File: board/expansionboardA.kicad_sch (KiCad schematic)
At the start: 58 parts, among them IC1 IS61WV25616EDBLL-10TLI, J1 USB_C_Receptacle, J2 USB_A_Stacked, J3 HDMI_A, J4 FAN, J5 DEBUG, U1 MAX3420EECJ, U2 GPIO_U2, U4 GPIO_U4, U6 CS4344-CZZR, U7 MAX3421EEHJ+T, Y1 Crystal, Y2 Crystal

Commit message: Updated board files
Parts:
- removed IC1: IS61WV25616EDBLL-10TLI, SOP80P1176X120-44N, symbol IS61WV25616EDBLL-10TLI:IS61WV25616EDBLL-10TLI
- added JP1: Jumper_2_Open, Jumper:SolderJumper-2_P1.3mm_Open_RoundedPad1.0x1.5mm, symbol Jumper:Jumper_2_Open
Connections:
- net 5V: now also JP1.2 (B)
- net GND: now also J3.11 (CKS), J3.2 (D2S), J3.5 (D1S), J3.8 (D0S), J3.SH
- net RIGHTOUT: no longer LSRIGHT1.P
- net speakerout: now reaches AU1.2, C9.1, R8.2
- net speakerout: now also LSRIGHT1.P
- net SRA0: no longer names the net of U2.34 (Pin_34)
- net SRA1: no longer names the net of U2.33 (Pin_33)
- net SRA10: no longer names the net of U4.10 (Pin_10)
- net SRA11: no longer names the net of U4.9 (Pin_9)
- net SRA12: no longer names the net of U4.12 (Pin_12)
- net SRA13: no longer names the net of U4.11 (Pin_11)
- net SRA14: no longer names the net of U4.14 (Pin_14)
- net SRA15: no longer names the net of U4.26 (Pin_26)
- net SRA16: no longer names the net of U4.25 (Pin_25)
- net SRA17: no longer names the net of U4.28 (Pin_28)
- net SRA2: no longer names the net of U2.32 (Pin_32)
- net SRA3: no longer names the net of U2.31 (Pin_31)
- net SRA4: no longer names the net of U2.30 (Pin_30)
- net SRA5: no longer names the net of U2.19 (Pin_19)
- net SRA6: no longer names the net of U2.18 (Pin_18)
- net SRA7: no longer names the net of U2.17 (Pin_17)
- net SRA8: no longer names the net of U2.16 (Pin_16)
- net SRA9: no longer names the net of U2.15 (Pin_15)
- net SRCEn: no longer names the net of U2.29 (Pin_29)
- net SRD0: no longer names the net of U2.28 (Pin_28)
- net SRD1: no longer names the net of U2.27 (Pin_27)
- net SRD10: no longer names the net of U4.15 (Pin_15)
- net SRD11: no longer names the net of U4.18 (Pin_18)
- net SRD12: no longer names the net of U4.17 (Pin_17)
- net SRD13: no longer names the net of U4.20 (Pin_20)
- net SRD14: no longer names the net of U4.19 (Pin_19)
- net SRD15: no longer names the net of U4.22 (Pin_22)
- net SRD2: no longer names the net of U2.26 (Pin_26)
- net SRD3: no longer names the net of U2.25 (Pin_25)
- net SRD4: no longer names the net of U2.24 (Pin_24)
- net SRD5: no longer names the net of U2.23 (Pin_23)
- net SRD6: no longer names the net of U2.22 (Pin_22)
- net SRD7: no longer names the net of U2.21 (Pin_21)
- net SRD8: no longer names the net of U4.13 (Pin_13)
- net SRD9: no longer names the net of U4.16 (Pin_16)
- net SRLB: no longer names the net of U4.21 (Pin_21)
- net SROE: no longer names the net of U4.23 (Pin_23)
- net SRUB: no longer names the net of U4.24 (Pin_24)
- net SRWE: no longer names the net of U2.20 (Pin_20)
- net n/c: no longer names the net of J3.18 (+5V)
- net n/c: now also JP1.1 (A)
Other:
- note removed: "SRAM"

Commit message: Board issue 2A with HDMI chip
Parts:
- removed JP1: Jumper_2_Open, Jumper:SolderJumper-2_P1.3mm_Open_RoundedPad1.0x1.5mm, symbol Jumper:Jumper_2_Open
- added JP1, JP2, JP3, JP4, JP5: Jumper_3_Open, Jumper:SolderJumper-3_P1.3mm_Open_RoundedPad1.0x1.5mm, symbol Jumper:Jumper_3_Open
- added R15, R18, R19, R20, R21, R22: 10KOhm, Resistor_SMD:R_0603_1608Metric_Pad0.98x0.95mm_HandSolder, symbol Device:R
- added R23: 33KOhm, Resistor_SMD:R_0603_1608Metric_Pad0.98x0.95mm_HandSolder, symbol Device:R
- added R24: 510Ohm, Resistor_SMD:R_0603_1608Metric_Pad0.98x0.95mm_HandSolder, symbol Device:R
- added U3: SII164CTG64, SI164CTG64:QFP50P1200X1200X120-64N, symbol SII164CTG64:SII164CTG64
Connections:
- net 5V: now also JP1.3 (B)
- net CK_N: now also U3.21 (TXC-); no longer U4.50 (Pin_50)
- net CK_P: now also U3.22 (TXC+); no longer U4.49 (Pin_49)
- net D0_N: now also U3.24 (TX0-); no longer U4.52 (Pin_52)
- net D0_P: now also U3.25 (TX0+); no longer U4.51 (Pin_51)
- net D1_N: now also U3.27 (TX1-); no longer U4.48 (Pin_48)
- net D1_P: now also U3.28 (TX1+); no longer U4.47 (Pin_47)
- net D2_N: now also U3.30 (TX2-); no longer U4.46 (Pin_46)
- net D2_P: now also U3.31 (TX2+); no longer U4.45 (Pin_45)
- net GND: now also JP2.1 (A), JP3.1 (A), JP4.1 (A), JP5.3 (B), R15.2, R19.2, U3.16 (GND), U3.17 (PGND), U3.20 (AGND), U3.26 (AGND__1), U3.32 (AGND__2), U3.48 (GND__1), U3.56 (IDCK-), U3.64 (GND__2)
- net REG3V3: now also JP1.1 (A), JP2.3 (B), JP3.3 (B), JP4.3 (B), R18.1, R20.2, R21.2, R22.2, R23.2, R24.2, U3.1 (VCC), U3.12 (VCC__1), U3.18 (PVCC1), U3.23 (AVCC), U3.29 (AVCC__1), U3.33 (VCC__2), U3.49 (PVCC2)
- net VRSTN: now reaches U4.12 (Pin_12)
- net VSCL: now reaches U4.14 (Pin_14)
- net VSDA: now reaches U4.16 (Pin_16)
- net VHOTPLUG: now reaches U4.18 (Pin_18)
- net VDKEN: now reaches U4.20 (Pin_20)
- net VDAT23: now reaches U4.25 (Pin_25)
- net VDAT23: now also U3.36 (D23)
- net VDAT22: now reaches U4.26 (Pin_26)
- net VDAT22: now also U3.37 (D22)
- net VDAT21: now reaches U4.27 (Pin_27)
- net VDAT21: now also U3.38 (D21)
- net VDAT20: now reaches U4.28 (Pin_28)
- net VDAT20: now also U3.39 (D20)
- net VDAT19: now reaches U4.29 (Pin_29)
- net VDAT19: now also U3.40 (D19)
- net VDAT18: now reaches U4.30 (Pin_30)
- net VDAT18: now also U3.41 (D18)
- net VDAT17: now reaches U4.31 (Pin_31)
- net VDAT17: now also U3.42 (D17)
- net VDAT16: now reaches U4.32 (Pin_32)
- net VDAT16: now also U3.43 (D16)
- net VDAT15: now reaches U4.33 (Pin_33)
- net VDAT15: now also U3.44 (D15)
- net VDAT14: now reaches U4.34 (Pin_34)
- net VDAT14: now also U3.45 (D14)
- net VDAT13: now reaches U4.35 (Pin_35)
- net VDAT13: now also U3.46 (D13)
- net VDAT12: now reaches U4.36 (Pin_36)
- net VDAT12: now also U3.47 (D12)
- net VDAT11: now reaches U4.37 (Pin_37)
- net VDAT11: now also U3.50 (D11)
- net VDAT10: now reaches U4.38 (Pin_38)
- net VDAT10: now also U3.51 (D10)
- net VDAT9: now reaches U4.39 (Pin_39)
- net VDAT9: now also U3.52 (D9)
- net VDAT8: now reaches U4.40 (Pin_40)
- net VDAT8: now also U3.53 (D8)
- net VDAT7: now reaches U4.41 (Pin_41)
- net VDAT7: now also U3.54 (D7)
- net VDAT6: now reaches U4.42 (Pin_42)
- net VDAT6: now also U3.55 (D6)
- net VDAT5: now reaches U4.43 (Pin_43)
- net VDAT5: now also U3.58 (D5)
- net VDAT4: now reaches U4.44 (Pin_44)
- net VDAT4: now also U3.59 (D4)
- net at J3.18 (+5V): now also JP1.2 (C)
- new net: JP3.2 (C), U3.7 (CTL2/A2/DK2)
- new net: R19.1, U3.15 (BSEL/SCL)
- new net: JP2.2 (C), U3.8 (CTL1/A1/DK1)
- new net: R24.1, U3.19 (EXT_SWING)
- new net: R20.1, U3.14 (DSEL/SDA)
- new net: JP5.1 (A), R21.1
- new net: JP5.2 (C), U3.35 (DKEN)
- new net: JP4.2 (C), U3.6 (CTL3/A3/DK3)
- new net: R18.2, U3.10 (~{PD})
- new net: R15.1, U3.13 (ISEL/~{RST})
- new net: R23.1, U3.3 (VREF)
- new net: R22.1, U3.9 (EDGE/HTPLG)
- new net VCLK: U3.57 (IDCK+), U4.49 (Pin_49)
- new net VDAT0: U3.63 (D0), U4.48 (Pin_48)
- new net VDAT1: U3.62 (D1), U4.47 (Pin_47)
- new net VDAT2: U3.61 (D2), U4.46 (Pin_46)
- new net VDAT3: U3.60 (D3), U4.45 (Pin_45)
- new net VDE: U3.2 (DE), U4.50 (Pin_50)
- new net VHSYNC: U3.4 (HSYNC), U4.51 (Pin_51)
- new net VVSYNC: U3.5 (VSYNC), U4.52 (Pin_52)
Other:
- note added: "HDMI out"
- note added: "Video Output"
- note removed: "DVI out over HDMI"
- moved on the sheet: C15, C16, C17, C18, C20, J2, R16, R17, U7, Y2

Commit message: Updating future board layout
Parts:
- removed LSRIGHT1: AS01508MS-SC11-WP-R, SPKR_AS01508MS-SC11-WP-R, symbol AS01508MS-SC11-WP-R:AS01508MS-SC11-WP-R
- removed Y1, Y2: Crystal, Crystal:Crystal_AT310_D3.0mm_L10.0mm_Horizontal, symbol Device:Crystal
- added Y1, Y2: 403C35D12M00000, 403C35D12M00000:XTAL_403C35D12M00000, symbol 403C35D12M00000:403C35D12M00000
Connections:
- net AU_LRCLK: now also U4.21 (Pin_21); no longer U2.41 (Pin_41)
- net AU_MCLK: now also U4.23 (Pin_23); no longer U2.43 (Pin_43)
- net AU_SCLK: now also U4.19 (Pin_19); no longer U2.39 (Pin_39)
- net AU_SDIN: now also U4.17 (Pin_17); no longer U2.37 (Pin_37)
- net GND: now also Y1.2 (GND), Y1.4 (GND__1), Y2.2 (GND), Y2.4 (GND__1)
- net LED0: now also U2.30 (Pin_30); no longer U2.59 (Pin_59)
- net LED1: now also U2.32 (Pin_32); no longer U2.57 (Pin_57)
- net LED2: now also U2.34 (Pin_34); no longer U2.55 (Pin_55)
- net LED3: now also U2.36 (Pin_36); no longer U2.53 (Pin_53)
- net at C3.2, U1.26 (XI): now also Y1.1
- net at C4.2, U1.27 (XO): now also Y1.3
- net at C15.2, U7.24 (XI): now also Y2.1
- net at C16.2, U7.25 (XO): now also Y2.3
- net VDKEN: no longer names the net of U4.20 (Pin_20)
- net VHOTPLUG: no longer names the net of U4.18 (Pin_18)
- net VRSTN: no longer names the net of U4.12 (Pin_12)
- net VSCL: no longer names the net of U4.14 (Pin_14)
- net VSDA: no longer names the net of U4.16 (Pin_16)
- net speakerout: no longer names the net of AU1.2, C9.1, R8.2
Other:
- note removed: "Onboard Speaker"
- moved on the sheet: C16, C3, C4, J4

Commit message: Switched to board revision 2B Removed built-in HDMI code, using external Lattice chip
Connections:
- net GND: now also U3.34 (RESERVED)
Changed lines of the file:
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@@
+    (stroke (width 0) (type default))
+  )
+  (wire (pts (xy 372.11 40.64) (xy 384.81 40.64))
     (stroke (width 0) (type default))
   )
@@
     (stroke (width 0) (type default))
   )
+  (wire (pts (xy 326.39 119.38) (xy 326.39 123.19))
+    (stroke (width 0) (type default))
+  )
   (wire (pts (xy 323.85 96.52) (xy 326.39 96.52))
     (stroke (width 0) (type default))
@@
   )
   (wire (pts (xy 86.36 48.26) (xy 86.36 57.15))
-    (stroke (width 0) (type default))
-  )
-  (wire (pts (xy 372.11 40.64) (xy 377.19 40.64))
     (stroke (width 0) (type default))
   )
@@
     (effects (font (size 1.27 1.27)) (justify right))
     (property "Intersheetrefs" "${INTERSHEET_REFS}" (at 33.0171 123.19 0)
+      (effects (font (size 1.27 1.27)) (justify right) hide)
+    )
+  )
+  (global_label "GND" (shape input) (at 326.39 123.19 270) (fields_autoplaced)
+    (effects (font (size 1.27 1.27)) (justify right))
+    (property "Intersheetrefs" "${INTERSHEET_REFS}" (at 326.39 129.0199 90)
       (effects (font (size 1.27 1.27)) (justify right) hide)
     )
@@
     )
   )
-  (global_label "REG3V3" (shape input) (at 377.19 40.64 0) (fields_autoplaced)
-    (effects (font (size 1.27 1.27)) (justify left))
-    (property "Intersheetrefs" "${INTERSHEET_REFS}" (at 387.2924 40.64 0)
-      (effects (font (size 1.27 1.27)) (justify left) hide)
-    )
+  (global_label "REG3V3" (shape input) (at 384.81 40.64 0) (fields_autoplaced)
+    (effects (font (size 1.27 1.27)) (justify left))
+    (property "Intersheetrefs" "${INTERSHEET_REFS}" (at 394.9124 40.64 0)
+      (effects (font (size 1.27 1.27)) (justify left) hide)
+    )

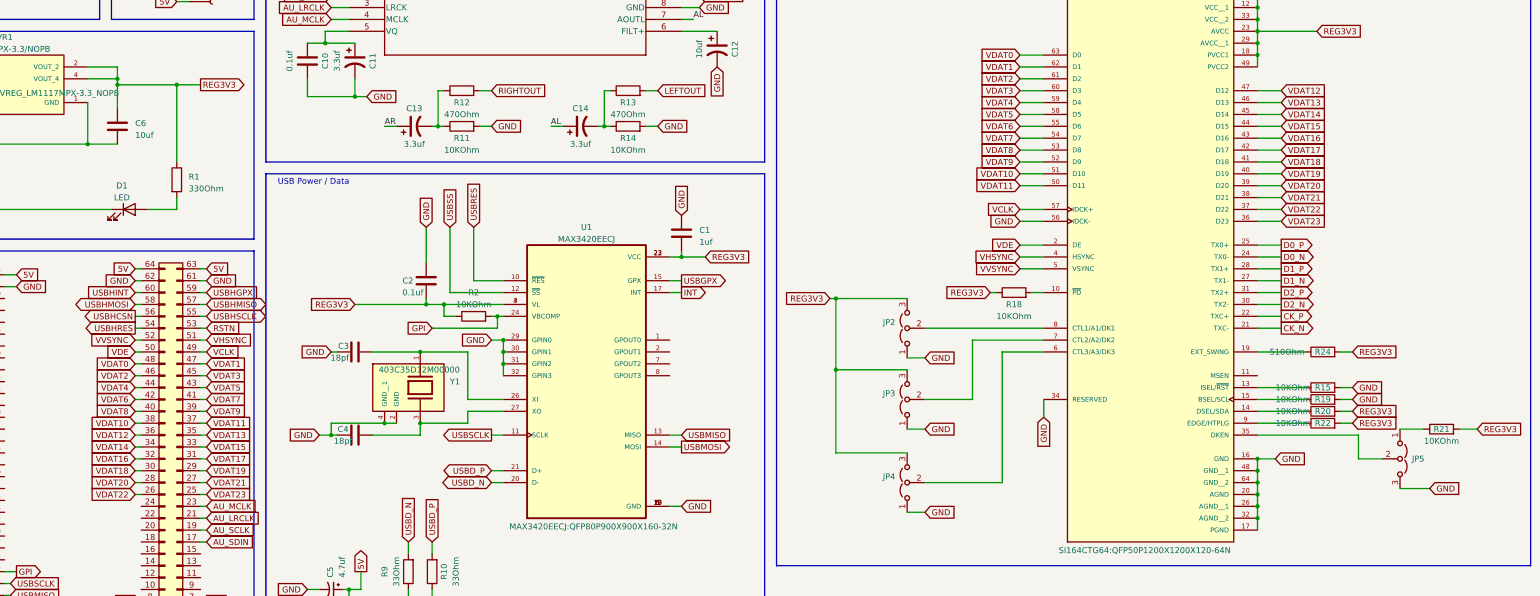
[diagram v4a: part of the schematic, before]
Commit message: Switched everything to 12bit RGB mode including the board design
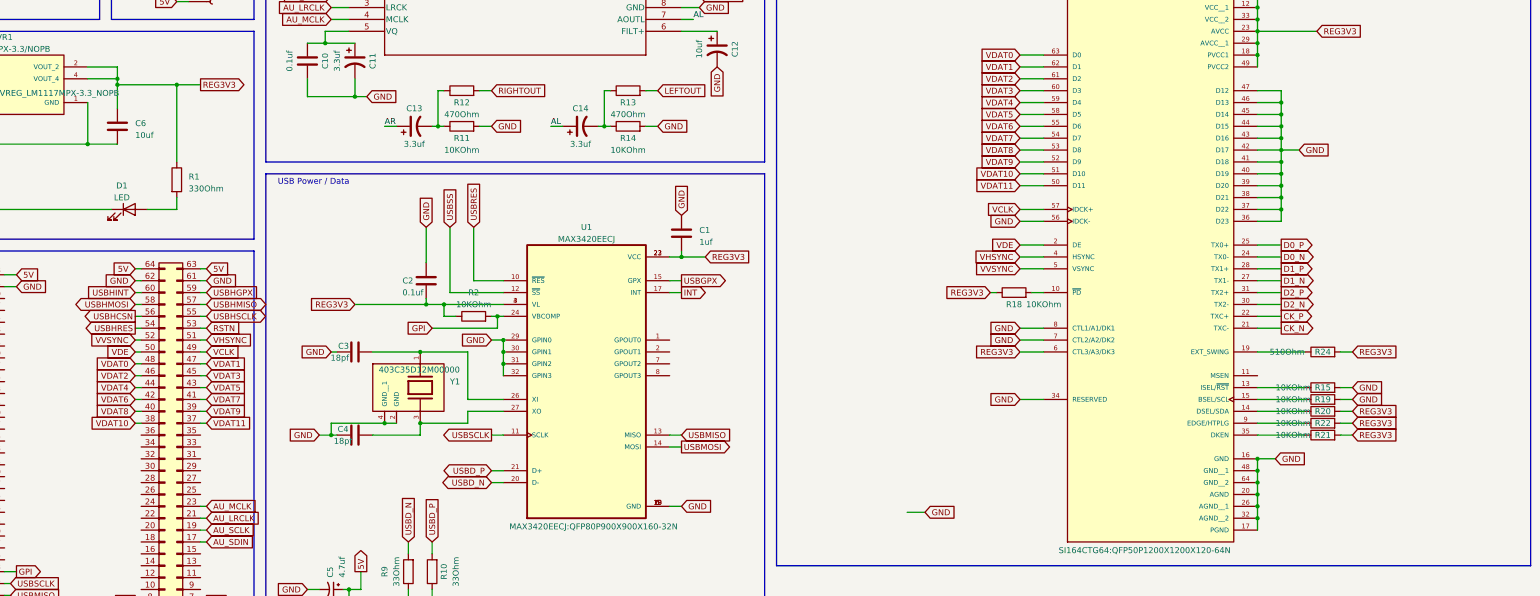
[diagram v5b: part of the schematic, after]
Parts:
- removed JP2, JP3, JP4, JP5: Jumper_3_Open, Jumper:SolderJumper-3_P1.3mm_Open_RoundedPad1.0x1.5mm, symbol Jumper:Jumper_3_Open
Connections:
- net GND: now also U3.36 (D23), U3.37 (D22), U3.38 (D21), U3.39 (D20), U3.40 (D19), U3.41 (D18), U3.42 (D17), U3.43 (D16), U3.44 (D15), U3.45 (D14), U3.46 (D13), U3.47 (D12), U3.7 (CTL2/A2/DK2), U3.8 (CTL1/A1/DK1)
- net REG3V3: now also U3.6 (CTL3/A3/DK3)
- net at R21.1: now also U3.35 (DKEN)
- net VDAT12: no longer names the net of U4.36 (Pin_36)
- net VDAT12: no longer U3.47 (D12)
- net VDAT13: no longer names the net of U4.35 (Pin_35)
- net VDAT13: no longer U3.46 (D13)
- net VDAT14: no longer names the net of U4.34 (Pin_34)
- net VDAT14: no longer U3.45 (D14)
- net VDAT15: no longer names the net of U4.33 (Pin_33)
- net VDAT15: no longer U3.44 (D15)
- net VDAT16: no longer names the net of U4.32 (Pin_32)
- net VDAT16: no longer U3.43 (D16)
- net VDAT17: no longer names the net of U4.31 (Pin_31)
- net VDAT17: no longer U3.42 (D17)
- net VDAT18: no longer names the net of U4.30 (Pin_30)
- net VDAT18: no longer U3.41 (D18)
- net VDAT19: no longer names the net of U4.29 (Pin_29)
- net VDAT19: no longer U3.40 (D19)
- net VDAT20: no longer names the net of U4.28 (Pin_28)
- net VDAT20: no longer U3.39 (D20)
- net VDAT21: no longer names the net of U4.27 (Pin_27)
- net VDAT21: no longer U3.38 (D21)
- net VDAT22: no longer names the net of U4.26 (Pin_26)
- net VDAT22: no longer U3.37 (D22)
- net VDAT23: no longer names the net of U4.25 (Pin_25)
- net VDAT23: no longer U3.36 (D23)
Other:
- moved on the sheet: R21

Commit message: Board and ROM updates
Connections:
- net GPI: now also U2.15 (Pin_15); no longer U2.13 (Pin_13)
- net INT: now also U2.23 (Pin_23); no longer U2.8 (Pin_8)
- net RSTN: now also U2.10 (Pin_10); no longer U4.53 (Pin_53)
- net USBGPX: now also U2.24 (Pin_24); no longer U2.7 (Pin_7)
- net USBHCSN: now also U4.58 (Pin_58); no longer U4.56 (Pin_56)
- net USBHGPX: now also U4.55 (Pin_55); no longer U4.59 (Pin_59)
- net USBHINT: now also U4.54 (Pin_54); no longer U4.60 (Pin_60)
- net USBHMOSI: now also U4.56 (Pin_56); no longer U4.58 (Pin_58)
- net USBHRES: now also U4.60 (Pin_60); no longer U4.54 (Pin_54)
- net USBHSCLK: now also U4.59 (Pin_59); no longer U4.55 (Pin_55)
- net USBMISO: now also U2.22 (Pin_22); no longer U2.9 (Pin_9)
- net USBMOSI: now also U2.21 (Pin_21); no longer U2.10 (Pin_10)
- net USBRES: now also U2.17 (Pin_17); no longer U2.14 (Pin_14)
- net USBSCLK: now also U2.20 (Pin_20); no longer U2.11 (Pin_11)
- net USBSS: now also U2.19 (Pin_19); no longer U2.12 (Pin_12)

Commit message: Board 2E wip
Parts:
- removed J5: DEBUG, Connector_PinSocket_2.54mm:PinSocket_1x04_P2.54mm_Vertical, symbol Connector:Conn_01x04_Socket
- removed RESETN1: SW_Push, SW_1-1825027-1, symbol 1-1825027-1:1-1825027-1
- VR1: symbol LM1117MPX-3.3_NOPB:LM1117MPX-3.3/NOPB -> LM1117MPX-3.3_NOPB:LM1117MPX-3.3/NOPB
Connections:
- net SHLD: now reaches CRD1.P1 (SHIELD), CRD1.P2 (SHIELD), CRD1.P3 (SHIELD), CRD1.P4 (SHIELD)
- net RSTN: no longer names the net of U2.10 (Pin_10)
- net UARTRX: no longer names the net of U2.44 (Pin_44)
- net UARTTX: no longer names the net of U2.42 (Pin_42)
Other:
- note removed: "DEBUG"
- note removed: "RESET"
- moved on the sheet: AU1, C1, C2, C3, C4, C5, C8, C9, J1, J4, R10, R2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

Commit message: More board updates
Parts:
- removed J4: FAN, Connector_PinHeader_2.54mm:PinHeader_1x02_P2.54mm_Vertical, symbol Connector_Generic:Conn_01x02
- removed JP1: Jumper_3_Open, Jumper:SolderJumper-3_P1.3mm_Open_RoundedPad1.0x1.5mm, symbol Jumper:Jumper_3_Open
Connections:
- net GPI: now also U4.14 (Pin_14); no longer U2.15 (Pin_15)
- net INT: now also U4.24 (Pin_24); no longer U2.23 (Pin_23)
- net LED0: now also U2.38 (Pin_38); no longer U2.30 (Pin_30)
- net LED1: now also U2.40 (Pin_40); no longer U2.32 (Pin_32)
- net LED2: now also U2.42 (Pin_42); no longer U2.34 (Pin_34)
- net LED3: now also U2.44 (Pin_44); no longer U2.36 (Pin_36)
- net USBGPX: now also U4.25 (Pin_25); no longer U2.24 (Pin_24)
- net USBMISO: now also U4.27 (Pin_27); no longer U2.22 (Pin_22)
- net USBMOSI: now also U4.26 (Pin_26); no longer U2.21 (Pin_21)
- net USBRES: now also U4.30 (Pin_30); no longer U2.17 (Pin_17)
- net USBSCLK: now also U4.29 (Pin_29); no longer U2.20 (Pin_20)
- net USBSS: now also U4.28 (Pin_28); no longer U2.19 (Pin_19)
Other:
- note removed: "FPGA Fan"
